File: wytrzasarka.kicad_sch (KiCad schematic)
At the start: 4 parts

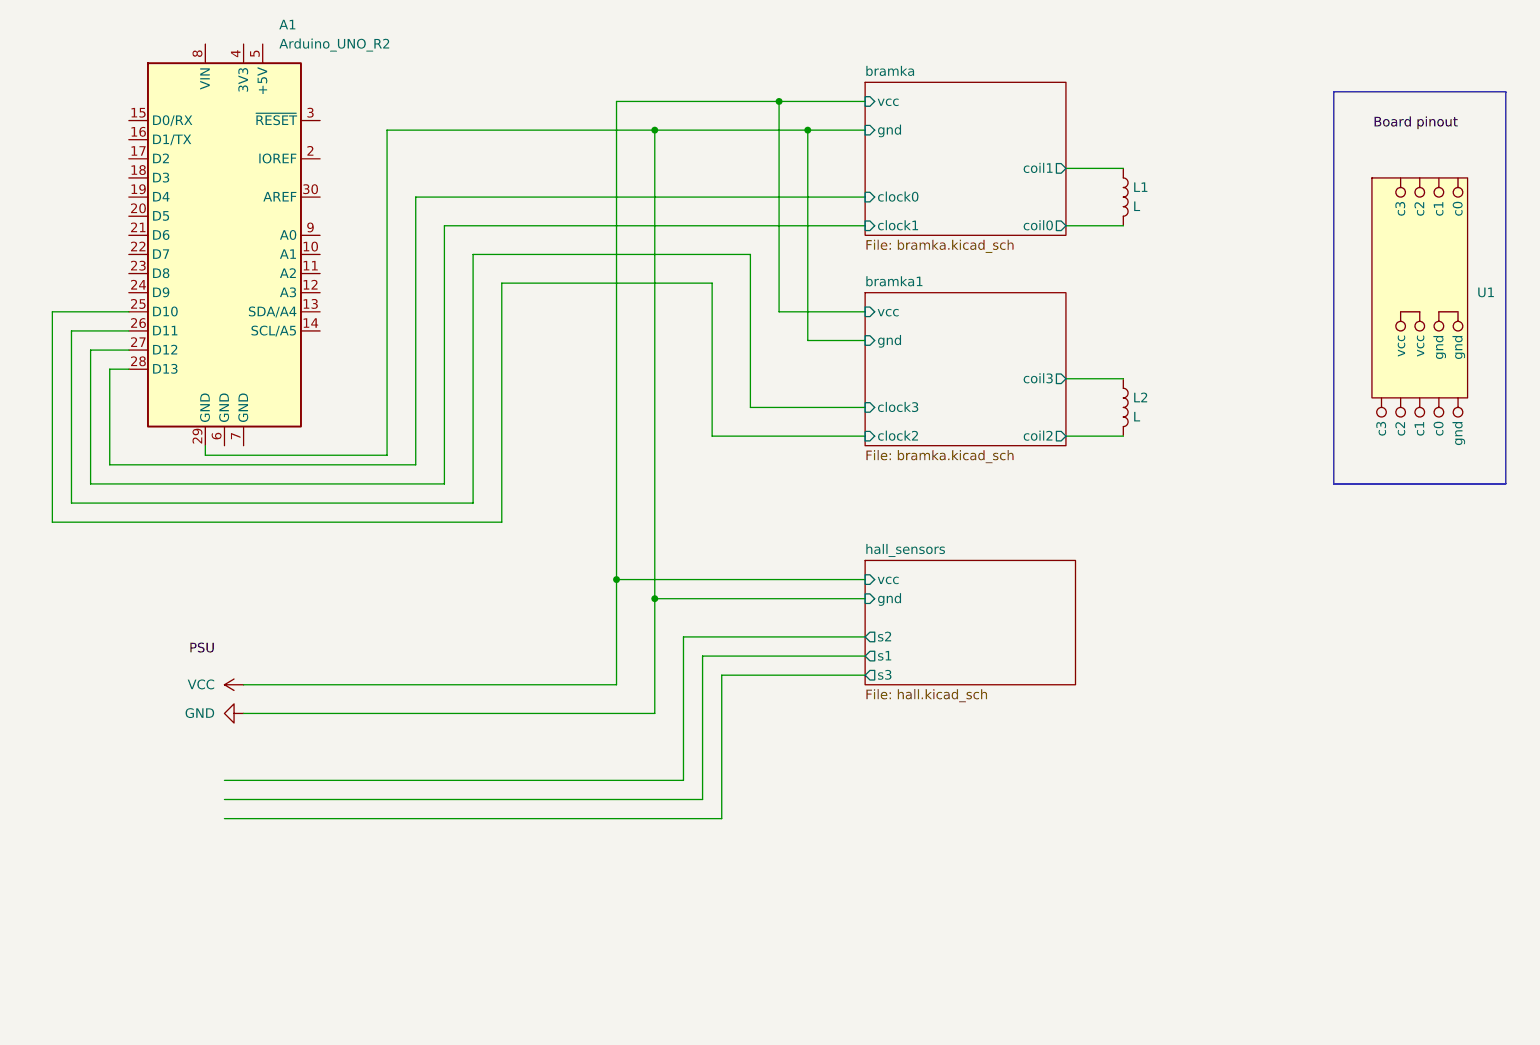
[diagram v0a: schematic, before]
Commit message: hall sensor voltage and pinout
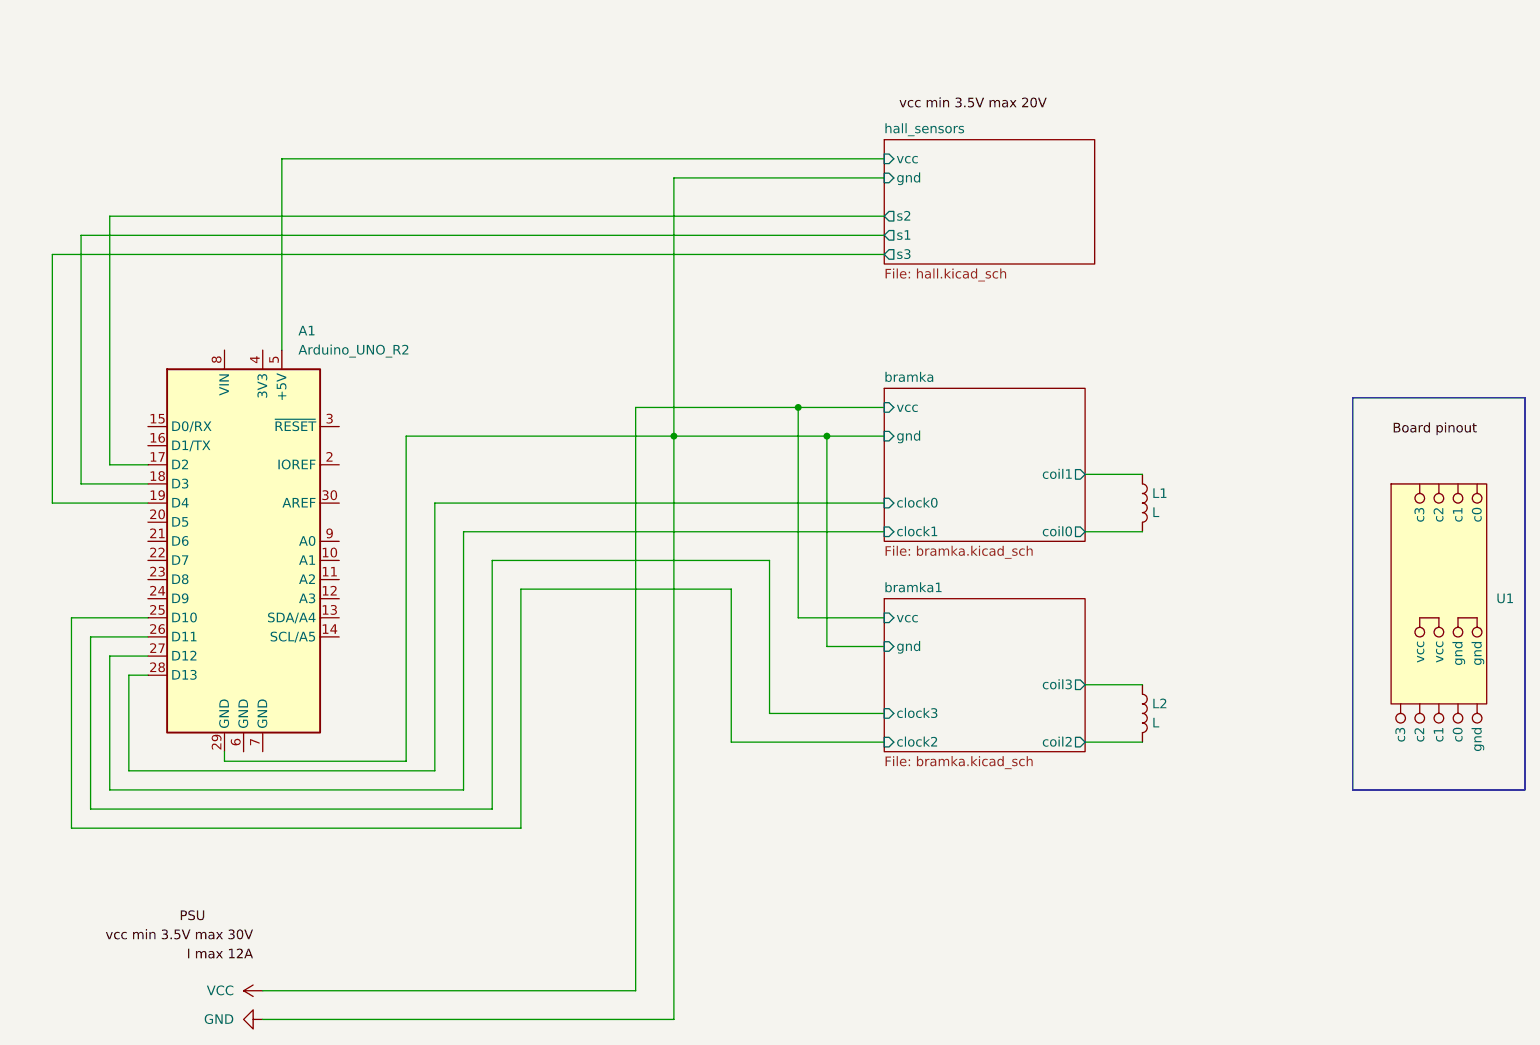
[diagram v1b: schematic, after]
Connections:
- net hall_sensors/s1: now also A1.18 (D3)
- net hall_sensors/s2: now also A1.17 (D2)
- net hall_sensors/s3: now also A1.19 (D4)
- net hall_sensors/vcc: now reaches A1.5 (+5V)
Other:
- moved on the sheet: A1, L1, L2, U1

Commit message: hall sensors pinout
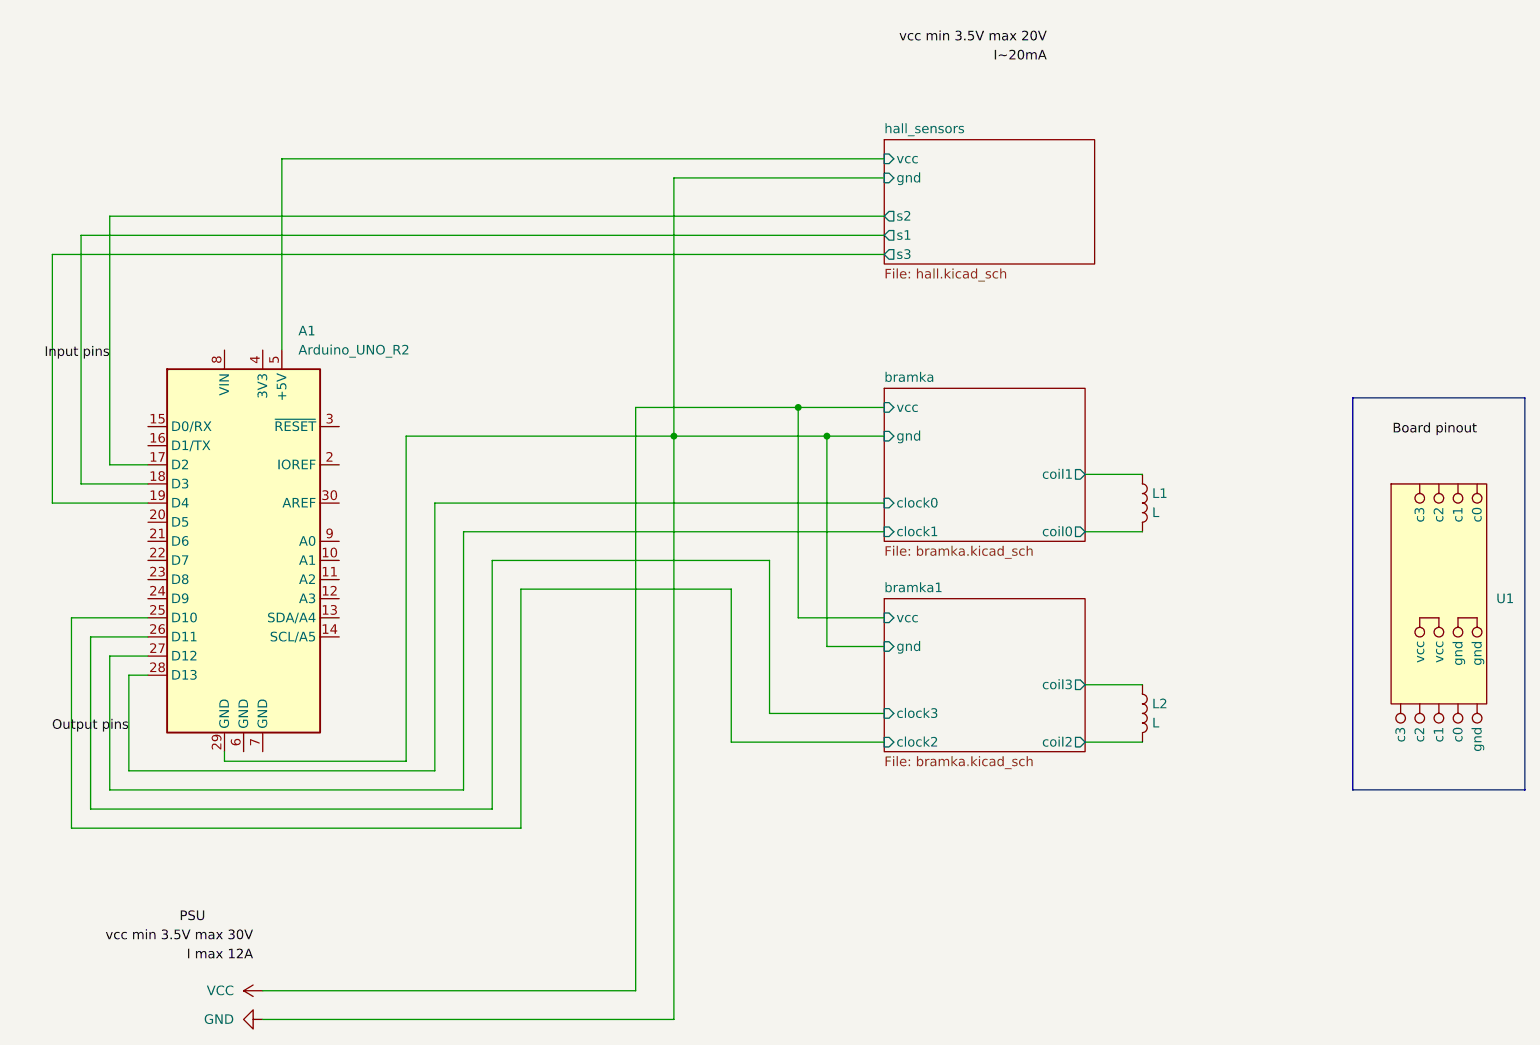
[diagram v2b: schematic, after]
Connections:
- net bramka/clock0 renamed Output pins
- net hall_sensors/s2 renamed Input pins
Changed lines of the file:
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@@
+	(wire
+		(pts
+			(xy 102.87 60.96) (xy 102.87 95.25)
+		)
+		(stroke
+			(width 0)
+			(type default)
+		)
+	)
 	(wire
 		(pts
@@
 	(wire
 		(pts
-			(xy 130.81 66.04) (xy 27.94 66.04)
-		)
-		(stroke
-			(width 0)
-			(type default)
-		)
-	)
-	(wire
-		(pts
 			(xy 157.48 135.89) (xy 165.1 135.89)
 		)
@@
 	(wire
 		(pts
+			(xy 27.94 66.04) (xy 130.81 66.04)
+		)
+		(stroke
+			(width 0)
+			(type default)
+		)
+	)
+	(wire
+		(pts
 			(xy 67.31 95.25) (xy 102.87 95.25)
 		)
@@
 	(wire
 		(pts
-			(xy 130.81 71.12) (xy 20.32 71.12)
-		)
-		(stroke
-			(width 0)
-			(type default)
-		)
-	)
-	(wire
-		(pts
 			(xy 22.86 147.32) (xy 22.86 119.38)
 		)
@@
 	(wire
 		(pts
+			(xy 24.13 68.58) (xy 130.81 68.58)
+		)
+		(stroke
+			(width 0)
+			(type default)
+		)
+	)
+	(wire
+		(pts
 			(xy 50.8 83.82) (xy 50.8 58.42)
 		)
@@
 	(wire
 		(pts
-			(xy 102.87 95.25) (xy 102.87 60.96)
-		)
-		(stroke
-			(width 0)
-			(type default)
-		)
-	)
-	(wire
-		(pts
 			(xy 43.18 138.43) (xy 67.31 138.43)
 		)
@@
 	(wire
 		(pts
-			(xy 24.13 68.58) (xy 130.81 68.58)
-		)
-		(stroke
-			(width 0)
-			(type default)
-		)
-	)
-	(wire
-		(pts
 			(xy 30.48 127) (xy 33.02 127)
 		)
@@
 		(pts
 			(xy 20.32 104.14) (xy 33.02 104.14)
+		)
+		(stroke
+			(width 0)
+			(type default)
+		)
+	)
+	(wire
+		(pts
+			(xy 20.32 71.12) (xy 130.81 71.12)
 		)
 		(stroke
@@
 		)
 	)
+	(label "I~20mA"
+		(at 152.4 45.72 180)
+		(fields_autoplaced yes)
+		(effects
+			(font
+				(size 1.27 1.27)
+			)
+			(justify right bottom)
+		)
+	)
 	(label "I max 12A"
 		(at 46.99 165.1 180)
@@
 	)
 	(label "vcc min 3.5V max 20V"
-		(at 152.4 52.07 180)
+		(at 152.4 43.18 180)
 		(fields_autoplaced yes)
 		(effects
@@
 		(fields_autoplaced yes)
 		(effects
+			(font
+				(size 1.27 1.27)
+			)
+			(justify right bottom)
+		)
+	)
+	(label "Input pins"
+		(at 27.94 85.09 180)
+		(fields_autoplaced yes)
+		(effects
+			(font
+				(size 1.27 1.27)
+			)
+			(justify right bottom)
+		)
+	)
+	(label "Output pins"
+		(at 30.48 134.62 180)
+		(fields_autoplaced yes)
+		(effects

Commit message: wojciechowe działania (poprawiono podschematy, dodano footprinty, pierwsze podejscie do pcb)
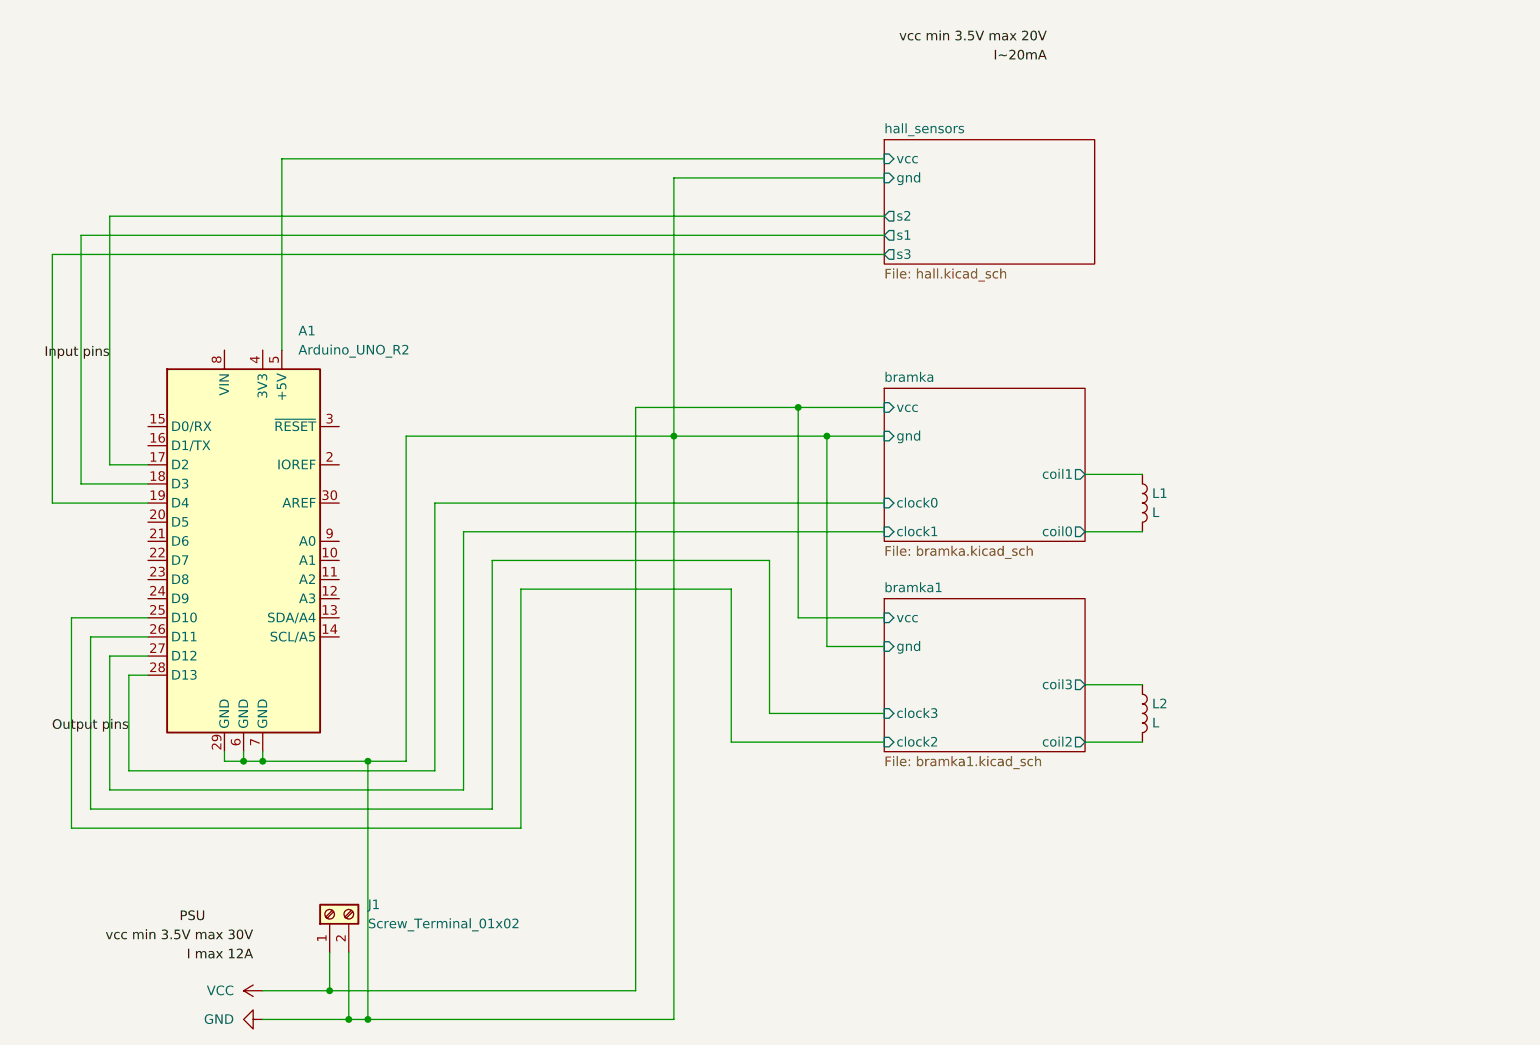
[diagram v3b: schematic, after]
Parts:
- removed U1: ~, symbol wytrzasarka-pinout:wytrzasarka
- added J1: Screw_Terminal_01x02, TerminalBlock:TerminalBlock_Xinya_XY308-2.54-2P_1x02_P2.54mm_Horizontal, symbol Connector:Screw_Terminal_01x02
- L1, L2: footprint (none) -> TerminalBlock:TerminalBlock_Xinya_XY308-2.54-2P_1x02_P2.54mm_Horizontal
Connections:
- net GND: now also A1.6 (GND), A1.7 (GND), J1.2 (Pin_2)
- net VCC: now also J1.1 (Pin_1)
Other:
- sheet bramka1: file bramka.kicad_sch -> bramka1.kicad_sch
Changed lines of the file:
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@@
+	)
+	(junction
+		(at 48.26 138.43)
+		(diameter 0)
+		(color 0 0 0 0)
 	)
 	(junction
@@
 	)
 	(junction
+		(at 59.69 172.72)
+		(diameter 0)
+		(color 0 0 0 0)
+	)
+	(junction
+		(at 57.15 168.91)
+		(diameter 0)
+		(color 0 0 0 0)
+	)
+	(junction
+		(at 45.72 138.43)
+		(diameter 0)
+		(color 0 0 0 0)
+	)
+	(junction
+		(at 62.23 138.43)
+		(diameter 0)
+		(color 0 0 0 0)
+	)
+	(junction
+		(at 62.23 172.72)
+		(diameter 0)
+		(color 0 0 0 0)
+	)
+	(junction
 		(at 123.19 95.25)
 		(diameter 0)
@@
 	(wire
 		(pts
+			(xy 59.69 172.72) (xy 62.23 172.72)
+		)
+		(stroke
+			(width 0)
+			(type default)
+		)
+	)
+	(wire
+		(pts
 			(xy 102.87 60.96) (xy 130.81 60.96)
 		)
@@
 	(wire
 		(pts
+			(xy 48.26 137.16) (xy 48.26 138.43)
+		)
+		(stroke
+			(width 0)
+			(type default)
+		)
+	)
+	(wire
+		(pts
+			(xy 62.23 172.72) (xy 102.87 172.72)
+		)
+		(stroke
+			(width 0)
+			(type default)
+		)
+	)
+	(wire
+		(pts
 			(xy 33.02 124.46) (xy 27.94 124.46)
 		)
@@
 	(wire
 		(pts
+			(xy 62.23 138.43) (xy 62.23 172.72)
+		)
+		(stroke
+			(width 0)
+			(type default)
+		)
+	)
+	(wire
+		(pts
 			(xy 110.49 135.89) (xy 110.49 115.57)
 		)
@@
 	(wire
 		(pts
-			(xy 48.26 168.91) (xy 97.79 168.91)
+			(xy 48.26 168.91) (xy 57.15 168.91)
 		)
 		(stroke
@@
 	(wire
 		(pts
+			(xy 48.26 138.43) (xy 62.23 138.43)
+		)
+		(stroke
+			(width 0)
+			(type default)
+		)
+	)
+	(wire
+		(pts
+			(xy 45.72 137.16) (xy 45.72 138.43)
+		)
+		(stroke
+			(width 0)
+			(type default)
+		)
+	)
+	(wire
+		(pts
 			(xy 50.8 58.42) (xy 130.81 58.42)
 		)
@@
 	(wire
 		(pts
-			(xy 43.18 138.43) (xy 67.31 138.43)
+			(xy 43.18 138.43) (xy 45.72 138.43)
 		)
 		(stroke
@@
 	(wire
 		(pts
+			(xy 62.23 138.43) (xy 67.31 138.43)
+		)
+		(stroke
+			(width 0)
+			(type default)
+		)
+	)
+	(wire
+		(pts
 			(xy 82.55 147.32) (xy 22.86 147.32)
 		)
@@
 	(wire
 		(pts
+			(xy 57.15 168.91) (xy 97.79 168.91)
+		)
+		(stroke
+			(width 0)
+			(type default)
+		)
+	)
+	(wire
+		(pts
 			(xy 24.13 101.6) (xy 24.13 68.58)
 		)
@@
 	(wire
 		(pts
+			(xy 45.72 138.43) (xy 48.26 138.43)
+		)
+		(stroke
+			(width 0)
+			(type default)
+		)
+	)
+	(wire
+		(pts
 			(xy 78.74 111.76) (xy 115.57 111.76)
 		)
@@
 	(wire
 		(pts
+			(xy 59.69 163.83) (xy 59.69 172.72)
+		)
+		(stroke
+			(width 0)
+			(type default)
+		)
+	)
+	(wire
+		(pts
 			(xy 27.94 66.04) (xy 27.94 99.06)
 		)
@@
 	(wire
 		(pts
-			(xy 48.26 172.72) (xy 102.87 172.72)
+			(xy 48.26 172.72) (xy 59.69 172.72)
 		)
 		(stroke
@@
 		)
 	)
-	(rectangle
-		(start 193.04 90.17)
-		(end 215.9 142.24)
-		(stroke
-			(width 0)
-			(type default)
-		)
-		(fill
-			(type none)
+	(wire
+		(pts
+			(xy 57.15 163.83) (xy 57.15 168.91)
+		)
+		(stroke
+			(width 0)
+			(type default)
 		)
 	)
@@
 	(label "vcc min 3.5V max 20V"
 		(at 152.4 43.18 180)
-		(fields_autoplaced yes)
-		(effects
-			(font
-				(size 1.27 1.27)
-			)
-			(justify right bottom)
-		)
-	)
-	(label "Board pinout"
-		(at 209.55 95.25 180)
 		(fields_autoplaced yes)
 		(effects
@@
 	)
 	(symbol
+		(lib_id "Connector:Screw_Terminal_01x02")
+		(at 57.15 158.75 90)
+		(unit 1)
+		(exclude_from_sim no)
+		(in_bom yes)
+		(on_board yes)
+		(dnp no)
+		(fields_autoplaced yes)
+		(property "Reference" "J1"
+			(at 62.23 157.4799 90)
+			(effects
+				(font
+					(size 1.27 1.27)
+				)
+				(justify right)
+			)
+		)
+		(property "Value" "Screw_Terminal_01x02"
+			(at 62.23 160.0199 90)
+			(effects
+				(font
+					(size 1.27 1.27)
+				)
+				(justify right)
+			)
+		)
+		(property "Footprint" "TerminalBlock:TerminalBlock_Xinya_XY308-2.54-2P_1x02_P2.54mm_Horizontal"
+			(at 57.15 158.75 0)
+			(effects
+				(font
+					(size 1.27 1.27)
+				)
+				(hide yes)
+			)
+		)
+		(property "Datasheet" "~"
+			(at 57.15 158.75 0)
+			(effects
+				(font
+					(size 1.27 1.27)
+				)
+				(hide yes)
+			)
+		)
+		(property "Description" "Generic screw terminal, single row, 01x02, script generated (kicad-library-utils/schlib/autogen/connector/)"
+			(at 57.15 158.75 0)
+			(effects
+				(font
+					(size 1.27 1.27)
+				)
+				(hide yes)
+			)
+		)
+		(pin "1"
+		)
+		(pin "2"
+		)
+		(instances
+			(project ""
+				(path "/fb8da07c-0c75-4bb9-88f5-d1eb037b3a33"
+					(reference "J1")
+					(unit 1)
+				)
+			)
+		)
+	)
+	(symbol
 		(lib_id "Device:L")
 		(at 165.1 104.14 0)
@@
 			)
 		)
-		(property "Footprint" ""
+		(property "Footprint" "TerminalBlock:TerminalBlock_Xinya_XY308-2.54-2P_1x02_P2.54mm_Horizontal"
 			(at 165.1 104.14 0)
 			(effects
@@
 				(path "/fb8da07c-0c75-4bb9-88f5-d1eb037b3a33"
 					(reference "L1")
-					(unit 1)
-				)
-			)
-		)
-	)
-	(symbol
-		(lib_id "wytrzasarka-pinout:wytrzasarka")
-		(at 207.01 123.19 0)
-		(unit 1)
-		(exclude_from_sim no)
-		(in_bom yes)
-		(on_board yes)
-		(dnp no)
-		(fields_autoplaced yes)
-		(property "Reference" "U1"
-			(at 212.09 116.8399 0)
-			(effects
-				(font
-					(size 1.27 1.27)
-				)
-				(justify left)
-			)
-		)
-		(property "Value" "~"
-			(at 212.09 118.745 0)
-			(effects
-				(font
-					(size 1.27 1.27)
-				)
-				(justify left)
-			)
-		)
-		(property "Footprint" ""
-			(at 207.01 123.19 0)
-			(effects
-				(font
-					(size 1.27 1.27)
-				)
-				(hide yes)
-			)
-		)
-		(property "Datasheet" ""
-			(at 207.01 123.19 0)
-			(effects
-				(font
-					(size 1.27 1.27)
-				)
-				(hide yes)
-			)
-		)
-		(property "Description" ""
-			(at 207.01 123.19 0)
-			(effects
-				(font
-					(size 1.27 1.27)
-				)
-				(hide yes)
-			)
-		)
-		(pin ""
-		)
-		(pin ""
-		)
-		(pin ""
-		)
-		(pin ""
-		)
-		(pin ""
-		)
-		(pin ""
-		)
-		(pin ""
-		)
-		(pin ""
-		)
-		(pin ""
-		)
-		(pin ""
-		)
-		(pin ""
-		)
-		(pin ""
-		)
-		(pin ""
-		)
-		(instances
-			(project ""
-				(path "/fb8da07c-0c75-4bb9-88f5-d1eb037b3a33"
-					(reference "U1")
 					(unit 1)
 				)
@@
 			)
 		)
-		(property "Footprint" ""
+		(property "Footprint" "TerminalBlock:TerminalBlock_Xinya_XY308-2.54-2P_1x02_P2.54mm_Horizontal"
 			(at 165.1 132.08 0)
 			(effects
@@
 			)
 		)
-		(property "Sheetfile" "bramka.kicad_sch"
+		(property "Sheetfile" "bramka1.kicad_sch"
 			(at 130.81 137.7446 0)
 			(effects
